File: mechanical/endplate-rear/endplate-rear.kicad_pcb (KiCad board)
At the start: 2 copper layers, 88 x 38 mm, 0 parts

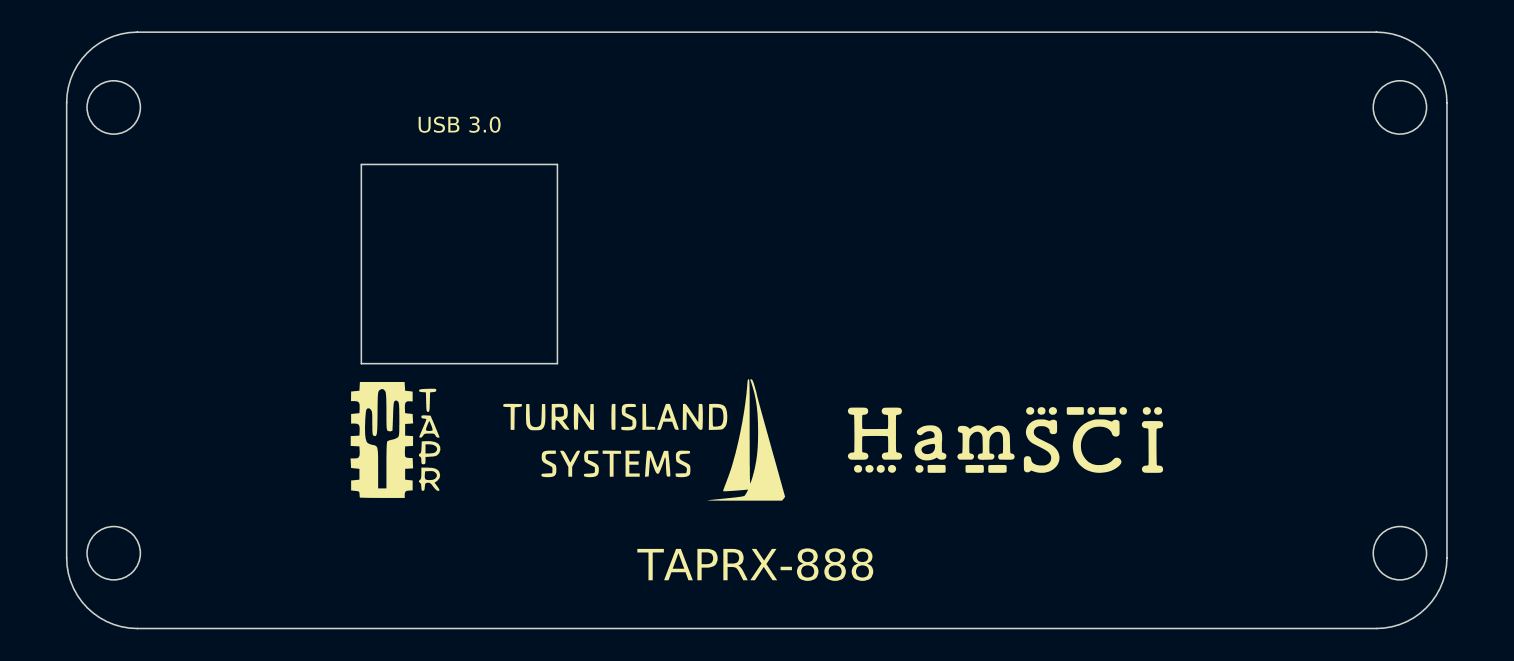
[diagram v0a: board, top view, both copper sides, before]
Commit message: mechanical: front logo-free; move all logos + expand title to rear
Per review: the front plate is now purely functional (SMA cutouts + function
labels + wordmark, no logos). The rear plate carries the branding -- all three
marks (TIS / HamSCI / TAPR) stacked in the area between the USB opening and the
right side -- and the 'TAPRX-888 HF SDR Receiver' silk line is raised and
enlarged to a proper title (size 1.6, same F.SilkS stroke font as the SMA labels).

Co-Authored-By: Claude Opus 4.8 <noreply@anthropic.com>
Claude-Session: https://claude.ai/code/session_019A4jkTeNPLki8CdfTWEUwM
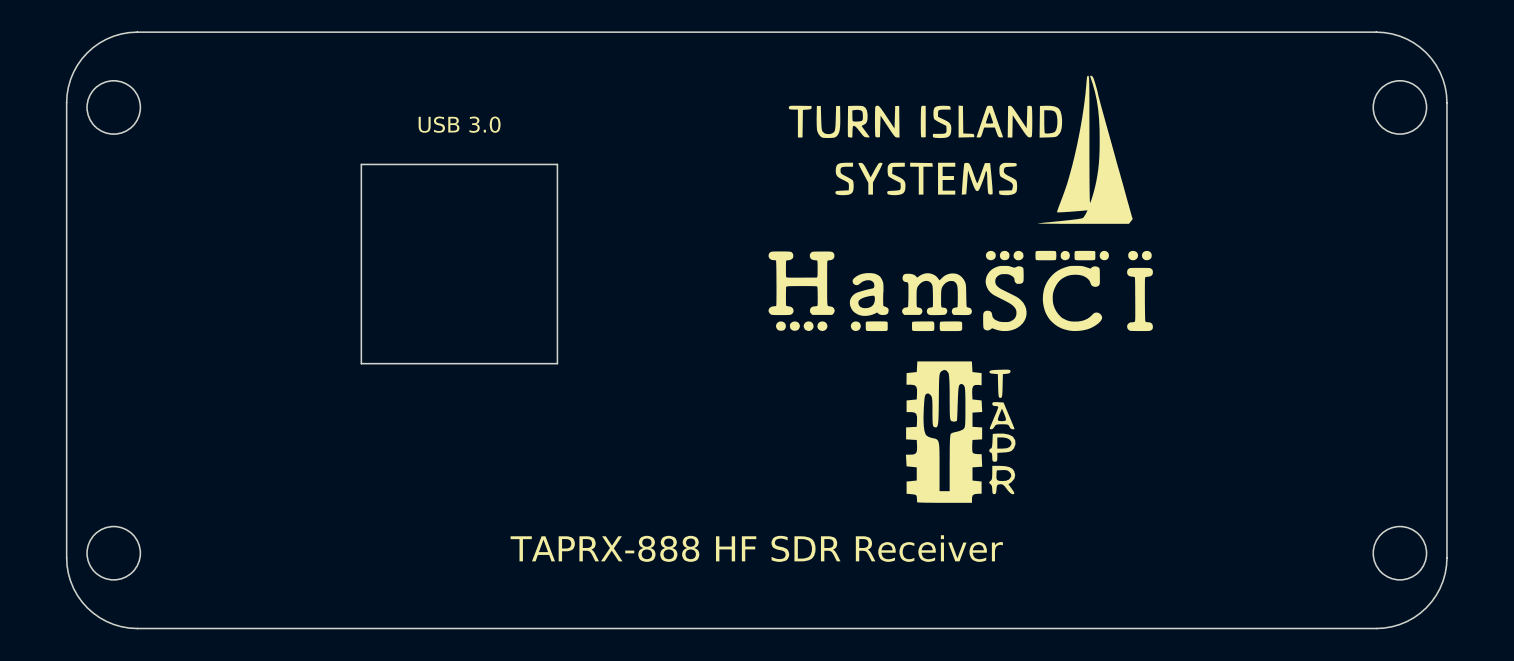
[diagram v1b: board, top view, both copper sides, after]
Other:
- board text added: "TAPRX-888 HF SDR Receiver"
- board text removed: "TAPRX-888"

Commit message: mechanical: logos to front mid-band, big TAPRX-888 title on rear
Per review: put the three logos (TAPR/TIS/HamSCI) on the FRONT, scaled 1.2 across
the open mid-band that was empty (X8-80, Y14-26), keeping the SMA cutouts, labels
and wordmark. The REAR drops the logos entirely and uses the open area below the
USB opening for a large two-line silk title: 'TAPRX-888' (size 3.5) over
'HF SDR Receiver' (size 1.6), same F.SilkS stroke font as the connector labels.

Co-Authored-By: Claude Opus 4.8 <noreply@anthropic.com>
Claude-Session: https://claude.ai/code/session_019A4jkTeNPLki8CdfTWEUwM
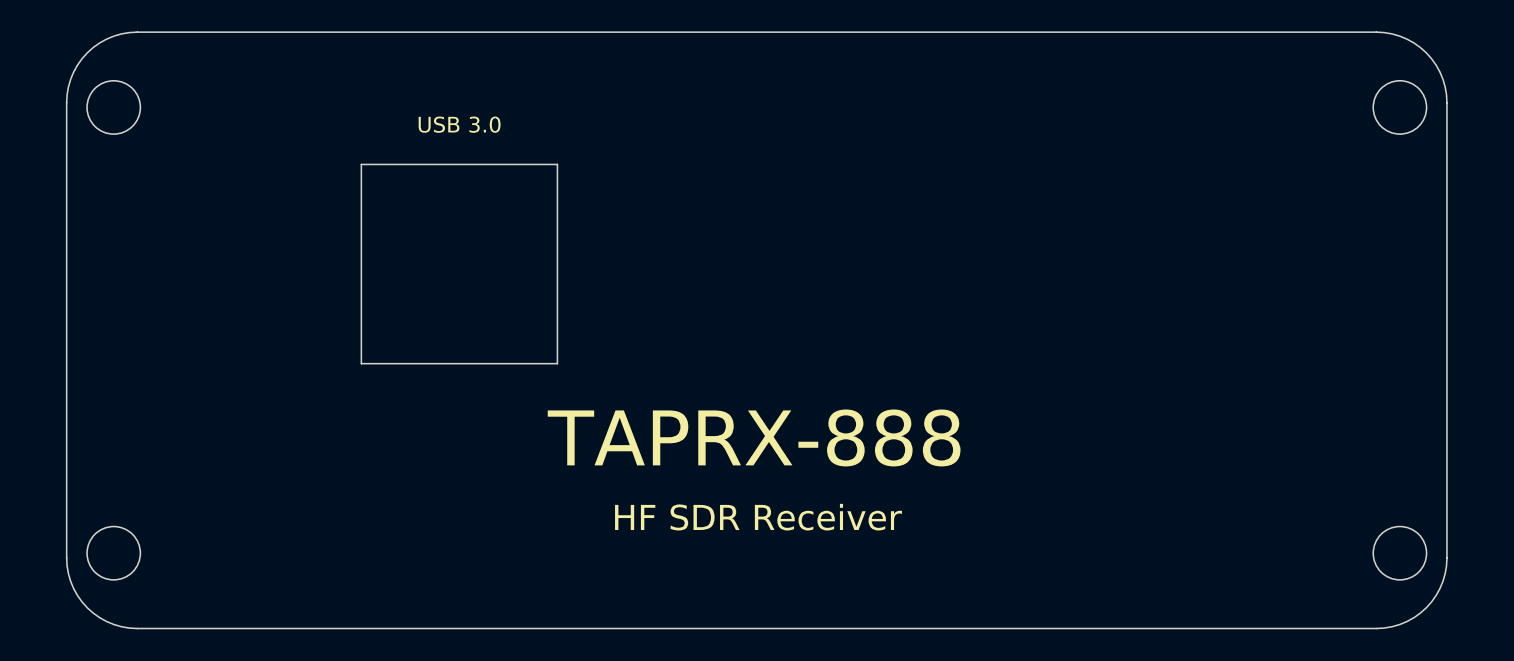
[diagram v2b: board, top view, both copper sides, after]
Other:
- board text added: "HF SDR Receiver"
- board text added: "TAPRX-888"
- board text removed: "TAPRX-888 HF SDR Receiver"

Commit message: mechanical: rear title on one line, sized to fit the plate width
Merge the rear title to a single silk line 'TAPRX-888 HF SDR Receiver' at size
3.7 (~72mm wide, centred, clear of the corner holes) -- the largest one-line
size the 88mm plate width allows. A true 50%-over-3.5 (5.25) one-liner would run
~105mm and overrun the plate, so width is the cap here.

Co-Authored-By: Claude Opus 4.8 <noreply@anthropic.com>
Claude-Session: https://claude.ai/code/session_019A4jkTeNPLki8CdfTWEUwM
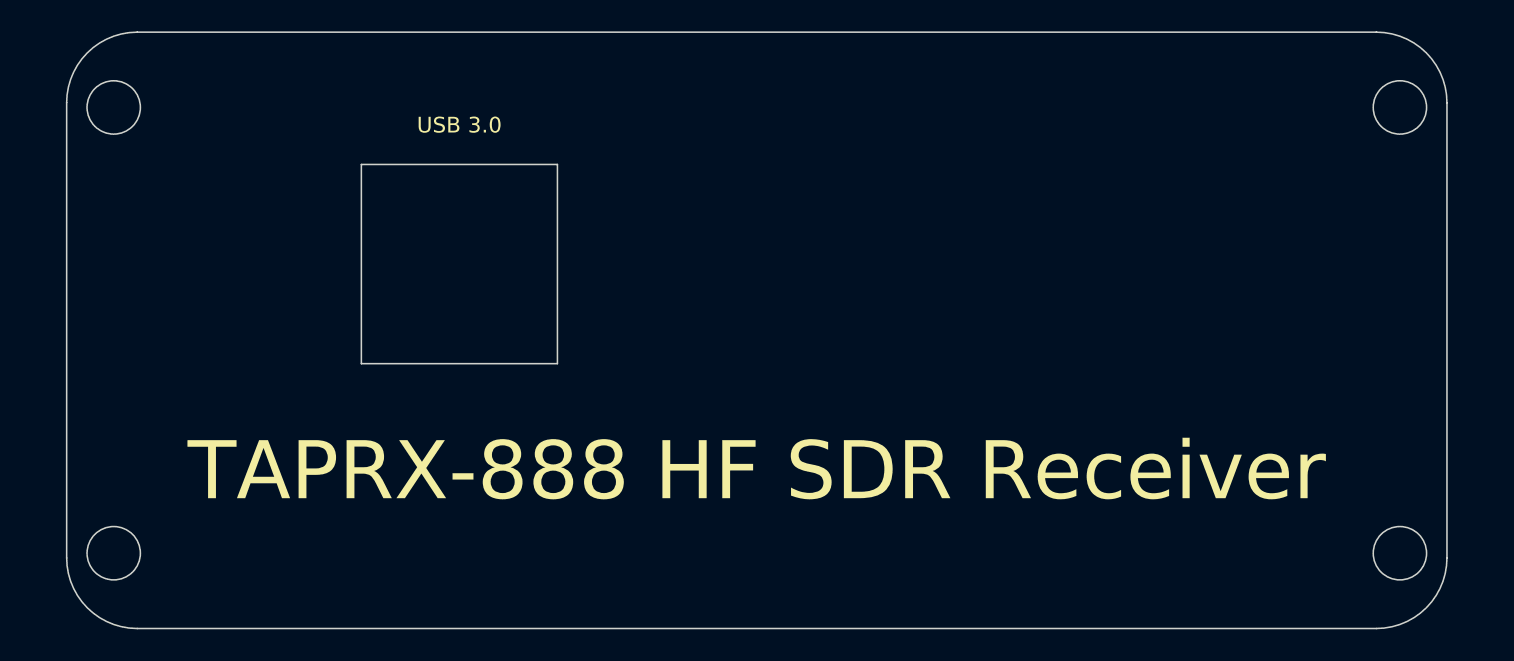
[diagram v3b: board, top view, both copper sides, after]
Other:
- board text added: "TAPRX-888 HF SDR Receiver"
- board text removed: "HF SDR Receiver"
- board text removed: "TAPRX-888"
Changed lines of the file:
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@@
 		)
 	)
-	(gr_text "TAPRX-888"
-		(at 44.0 26.0)
+	(gr_text "TAPRX-888 HF SDR Receiver"
+		(at 44.0 28.0)
 		(layer "F.SilkS")
 		(effects
 			(font
-				(size 3.5 3.5)
-				(thickness 0.5)
+				(size 3.7 3.7)
+				(thickness 0.55)
 			)
 		)
-	)
-	(gr_text "HF SDR Receiver"
-		(at 44.0 31.0)
-		(layer "F.SilkS")
-		(effects
-			(font
-				(size 1.6 1.6)
-				(thickness 0.24)
-			)
-		)
